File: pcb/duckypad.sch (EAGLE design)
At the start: 161 parts, among them IC2 REG1117, SW1 SPST_TACT-EVQQ2, SW2 SPST_TACT-EVQQ2, SW21 EC12E_SW, SW22 EC12E_SW, SW3 324_SW324_SWITCH_FOOT_HOLE, SW4 324_SW324_SWITCH_FOOT_HOLE, U1 USBC_16P, U2 USBC_16P, U3 ESP32-S3FN8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

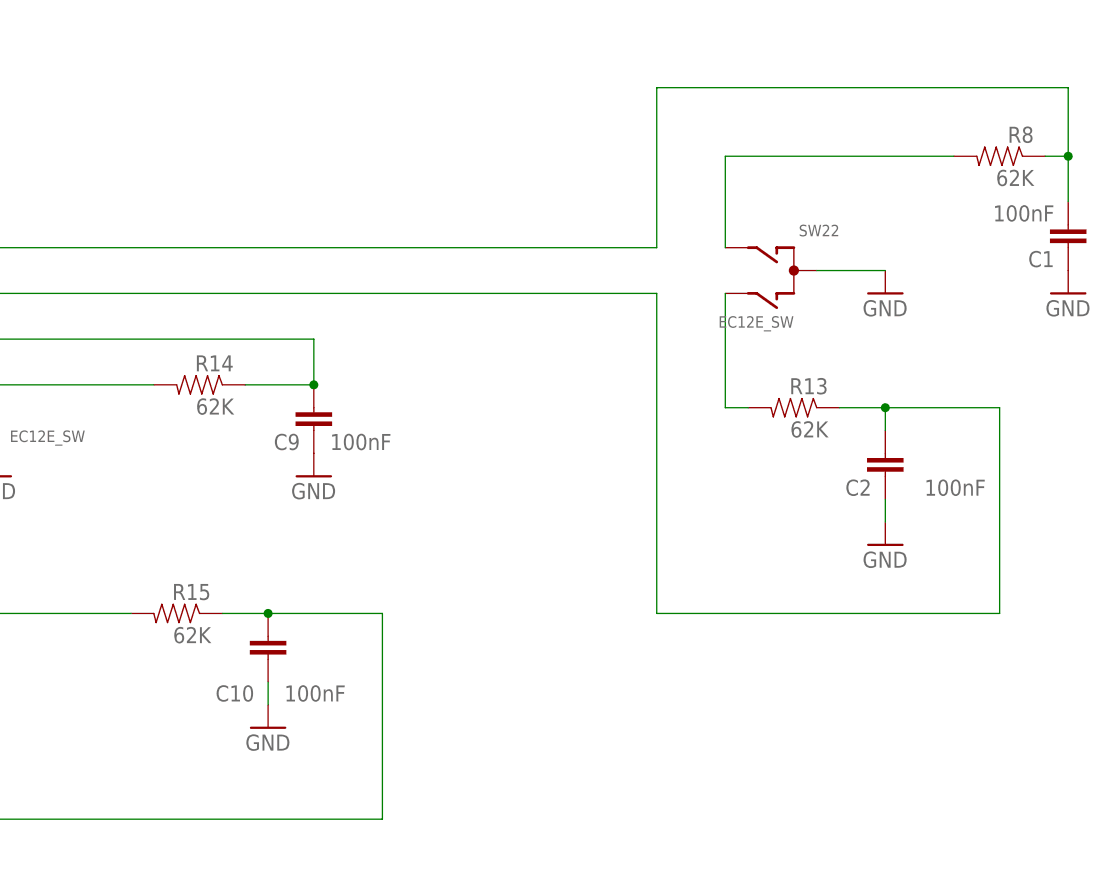
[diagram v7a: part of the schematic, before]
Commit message: adjusted rotary encoder rc circuit
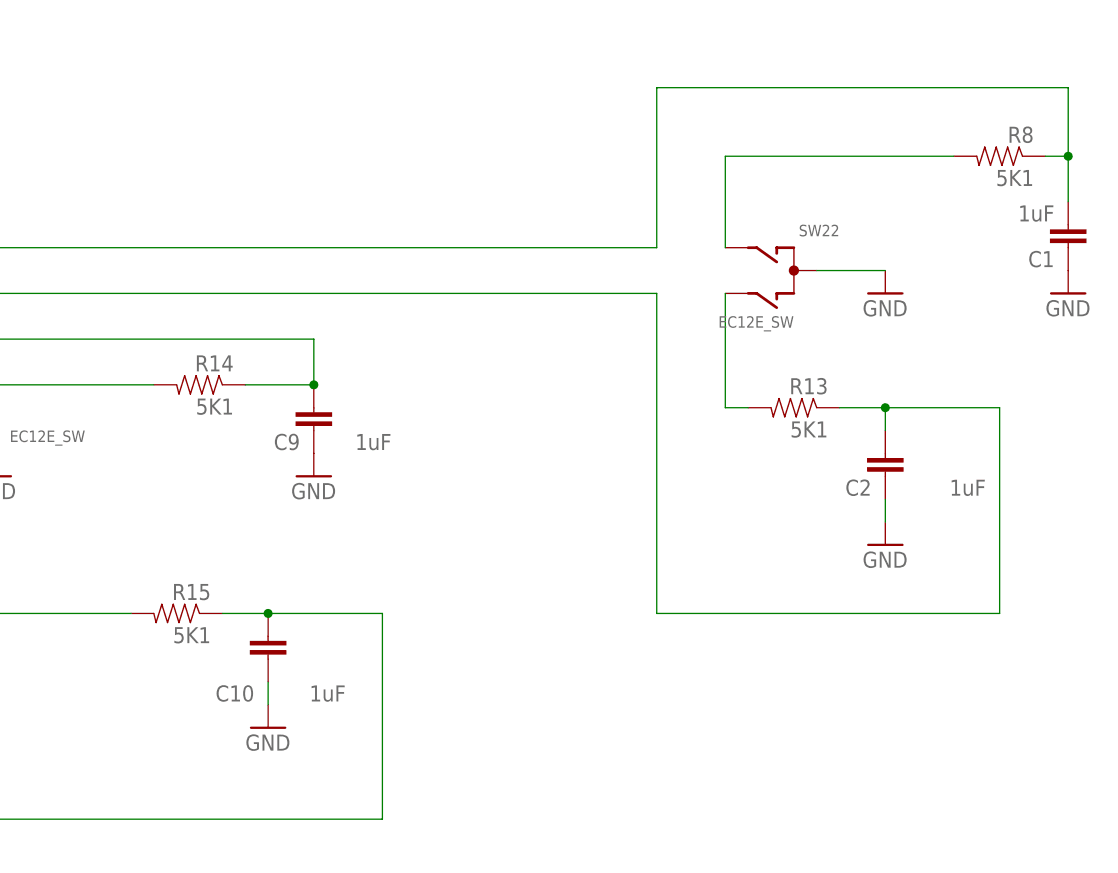
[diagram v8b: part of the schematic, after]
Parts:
- C1, C10, C2, C9: value 100nF -> 1uF
- R13, R14, R15, R8: value 62K -> 5K1
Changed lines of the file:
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@@
 <part name="GND55" library="supply1" library_urn="urn:adsk.eagle:library:371" deviceset="GND" device=""/>
 <part name="GND56" library="supply1" library_urn="urn:adsk.eagle:library:371" deviceset="GND" device=""/>
-<part name="C1" library="clock" deviceset="CAP" device="0805" value="100nF"/>
-<part name="R8" library="joyAnalog" deviceset="RESISTOR" device="0805-RES" value="62K"/>
+<part name="C1" library="clock" deviceset="CAP" device="0805" value="1uF"/>
+<part name="R8" library="joyAnalog" deviceset="RESISTOR" device="0805-RES" value="5K1"/>
 <part name="GND57" library="supply1" library_urn="urn:adsk.eagle:library:371" deviceset="GND" device=""/>
-<part name="R13" library="joyAnalog" deviceset="RESISTOR" device="0805-RES" value="62K"/>
-<part name="C2" library="clock" deviceset="CAP" device="0805" value="100nF"/>
+<part name="R13" library="joyAnalog" deviceset="RESISTOR" device="0805-RES" value="5K1"/>
+<part name="C2" library="clock" deviceset="CAP" device="0805" value="1uF"/>
 <part name="GND58" library="supply1" library_urn="urn:adsk.eagle:library:371" deviceset="GND" device=""/>
-<part name="R14" library="joyAnalog" deviceset="RESISTOR" device="0805-RES" value="62K"/>
-<part name="C9" library="clock" deviceset="CAP" device="0805" value="100nF"/>
+<part name="R14" library="joyAnalog" deviceset="RESISTOR" device="0805-RES" value="5K1"/>
+<part name="C9" library="clock" deviceset="CAP" device="0805" value="1uF"/>
 <part name="GND59" library="supply1" library_urn="urn:adsk.eagle:library:371" deviceset="GND" device=""/>
-<part name="R15" library="joyAnalog" deviceset="RESISTOR" device="0805-RES" value="62K"/>
-<part name="C10" library="clock" deviceset="CAP" device="0805" value="100nF"/>
+<part name="R15" library="joyAnalog" deviceset="RESISTOR" device="0805-RES" value="5K1"/>
+<part name="C10" library="clock" deviceset="CAP" device="0805" value="1uF"/>
 <part name="GND60" library="supply1" library_urn="urn:adsk.eagle:library:371" deviceset="GND" device=""/>
 <part name="R16" library="joyAnalog" deviceset="RESISTOR" device="0805-RES" value="10K"/>
